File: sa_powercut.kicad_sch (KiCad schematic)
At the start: 0 parts

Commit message: buck converter circuit
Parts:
- added Cff: 10pF, symbol Device:C
- added Cin, Cout: 22uF, symbol Device:C
- added Cinx, Coutx: 100nF, symbol Device:C
- added J1: Conn_01x02_Pin, symbol Connector:Conn_01x02_Pin
- added L1: 4.7uH, Package_SO:SOIC-16_3.9x9.9mm_P1.27mm, symbol Device:L
- added Renb: 30k, symbol Device:R
- added Rent: 210k, symbol Device:R
- added Rfbb: 30k, Package_DIP:DIP-8_W7.62mm, symbol Device:R
- added Rfbt: 220k, Package_DIP:DIP-8_W7.62mm, symbol Device:R
- added Rpg: 10k, Package_DIP:DIP-8_W7.62mm, symbol Device:R
- added U1: TPS564257DRLR, TPS564242DRLR_TEX, symbol sa_powercut_stuff:TPS564257DRLR
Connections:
- new net: Renb.1, Rent.2, U1.5 (EN)
- new net: Cff.2, Rfbb.2, Rfbt.2, U1.6 (FB)
- new net: Rpg.1, U1.4 (PG)
- new net: L1.1, U1.2 (SW)
- new net +12V: Cin.1, Cinx.1, J1.1 (Pin_1), Rent.1, U1.1 (VIN)
- new net +5V: Cff.1, Cout.1, Coutx.1, L1.2, Rfbt.1, Rpg.2
- new net GND: Cin.2, Cinx.2, Cout.2, Coutx.2, J1.2 (Pin_2), Renb.2, Rfbb.1, U1.3 (GND)

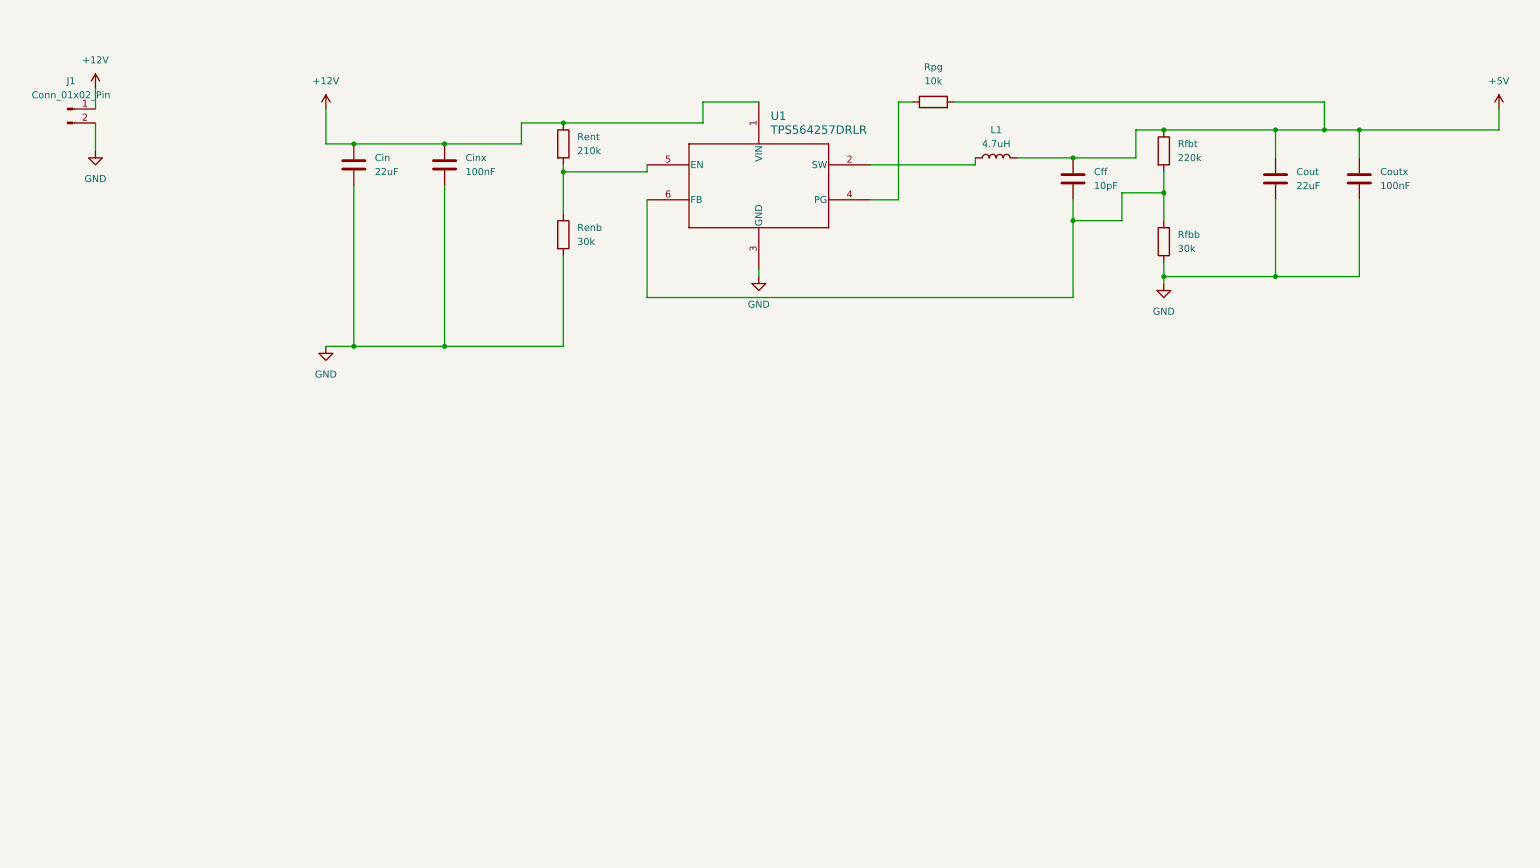
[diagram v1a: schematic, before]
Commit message: latch circuit/power interrupt
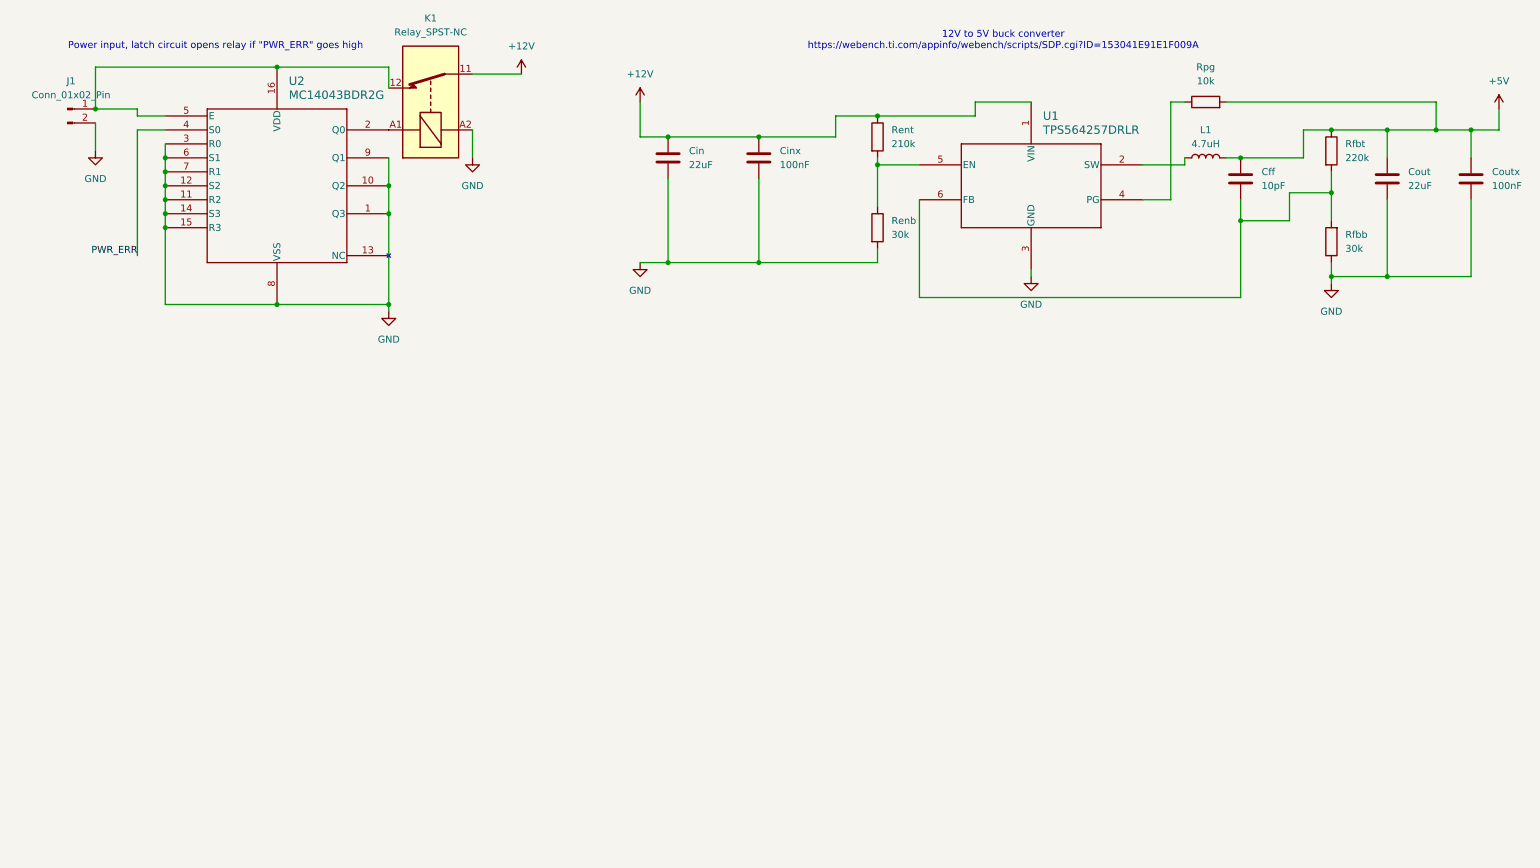
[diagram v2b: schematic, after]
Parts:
- added K1: Relay_SPST-NC, Relay_THT:Relay_SPST_Zettler-AZSR131, symbol Relay:Relay_SPST-NC
- added U2: MC14043BDR2G, SOIC-16_ONS, symbol sa_powercut_stuff:MC14043BDR2G
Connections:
- net +12V: now also K1.11; no longer J1.1 (Pin_1)
- net GND: now also K1.A2, U2.1 (Q3), U2.10 (Q2), U2.11 (R2), U2.12 (S2), U2.14 (S3), U2.15 (R3), U2.3 (R0), U2.6 (S1), U2.7 (R1), U2.8 (VSS), U2.9 (Q1)
- new net: J1.1 (Pin_1), K1.12, U2.16 (VDD), U2.5 (E)
- new net: K1.A1, U2.2 (Q0)
- new net PWR_ERR: U2.4 (S0)
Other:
- note added: "12V to 5V buck converter https://webench.ti.com/appinfo/webench/scripts/SDP.cgi?ID=153041E91E1F009A"
- note added: "Power input, latch circuit opens relay if "PWR_ERR" goes high"
- moved on the sheet: Cff, Cin, Cinx, Cout, Coutx, L1, Renb, Rent, Rfbb, Rfbt, Rpg, U1

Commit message: add zener diode
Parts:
- added R1: 100, Package_DIP:DIP-8_W7.62mm, symbol Device:R
- added U3: 1N5338BRLG, CASE_17AA-01_ONS, symbol sa_powercut_stuff:1N5338BRLG
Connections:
- net +5V: now also R1.1
- net PWR_ERR: now also U3.2
- new net: R1.2, U3.1
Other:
- note added: "Zener diode for overvoltage protection"

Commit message: hypothetical current protection
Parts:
- added C1: 0.1uF, DBV0006A_N, symbol Device:C
- added D1: D, SOT-25 SMV_TOS, symbol Device:D
- added D2: D, symbol Device:D
- added J2: Conn_01x02_Pin, symbol Connector:Conn_01x02_Pin
- added U4: TPS25221DBVR, DBV0006A_N, symbol sa_powercut_stuff:TPS25221DBVR
- added U5: TC4S584F_LF, SOT-25 SMV_TOS, symbol sa_powercut_stuff:TC4S584F_LF
- R1: value 100 -> 28k; footprint Package_DIP:DIP-8_W7.62mm -> (none)
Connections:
- net +5V: now also U3.1, C1.2, U4.1 (IN), U4.3 (EN), U5.5 (VDD); no longer R1.1
- net GND: now also R1.2, C1.1, J2.2 (Pin_2), U4.2 (GND), U5.3 (VSS)
- net PWR_ERR: now also D1.1 (K), D2.1 (K); no longer U3.2
- new net: J2.1 (Pin_1), U4.6 (OUT)
- new net: D1.2 (A), U3.2
- new net: R1.1, U4.5 (ILIM)
- new net: U4.4 (~{FAULT}), U5.2 (IN)
- new net: D2.2 (A), U5.4 (OUT)
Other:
- note added: "IC for overcurrent protection"
- note added: "TODO: resistor and error LED between relay coil and ground, need to figure out the resistance needed here"
- note added: "to slow antenna"
- company: (none) -> TTU Lightning Research Group
- title: (none) -> SANTA protected buck converter
